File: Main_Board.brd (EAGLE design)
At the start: 122.5 x 95.4 mm, 105 parts, among them J1 SERVO, J5 SPEAKER, J6 SDIO-SDCARD, P1 MOTOR_HEADER, P2 MOTOR_HEADER, P3 JTAG, U1 LMS8117, U10 IMU, U14 TPA2005D1DGN, U2 5V_BUCK_REG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

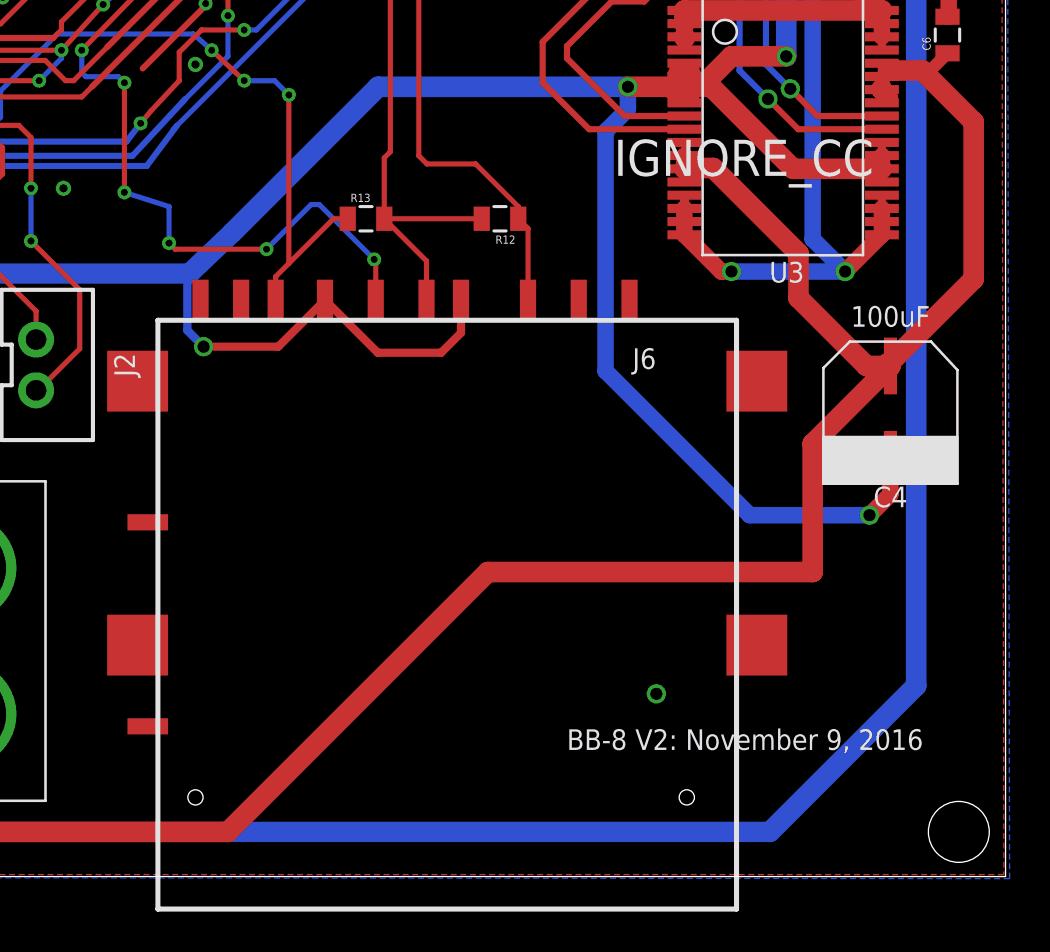
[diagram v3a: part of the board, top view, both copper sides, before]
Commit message: made SD card traces closer in length
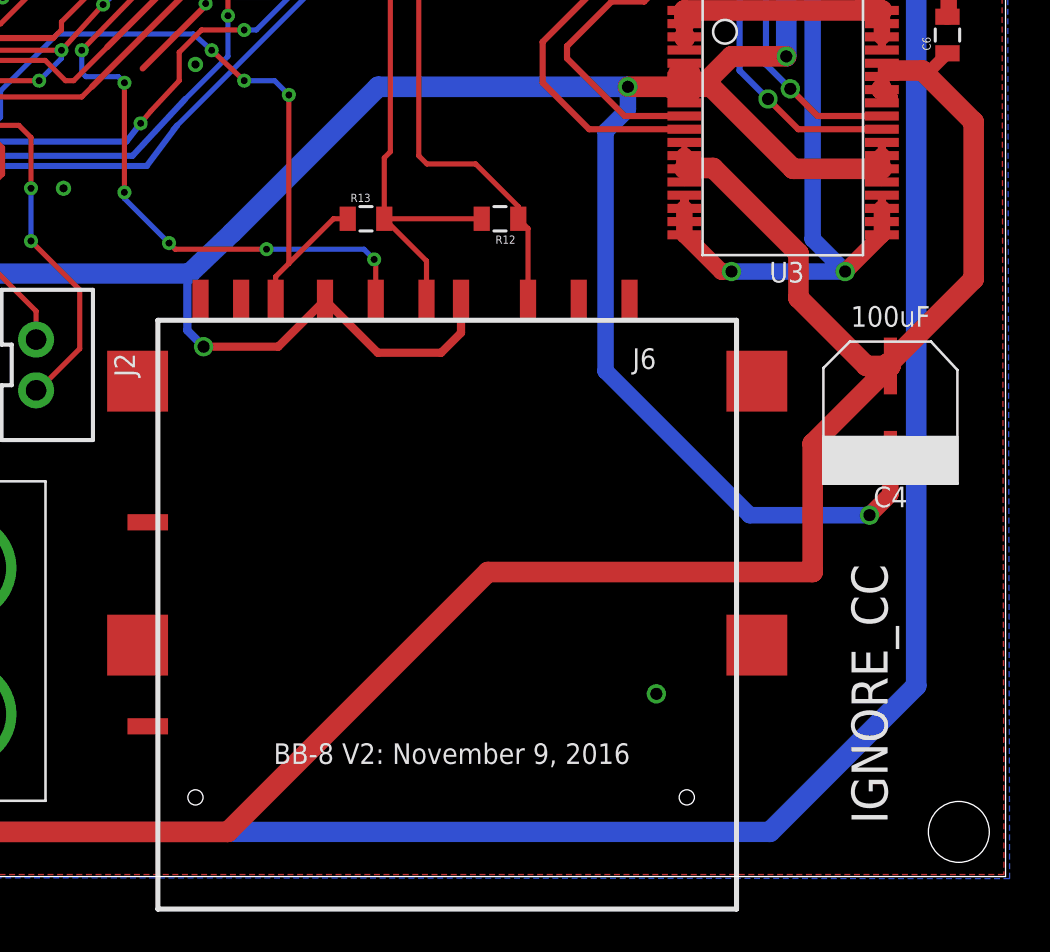
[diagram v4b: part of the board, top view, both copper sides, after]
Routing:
- net SDIO_CK: track 70.6 -> 68.1 mm
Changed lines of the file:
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@@
 <rectangle x1="15.5" y1="83.2" x2="20.7" y2="92.4" layer="41"/>
 <text x="41" y="65.6" size="1.778" layer="21" font="vector">REG_BOOT</text>
-<text x="103.210571875" y="34.512" size="1.778" layer="21" font="vector">IGNORE_CC</text>
+<text x="114.912" y="15.389428125" size="1.778" layer="21" font="vector" rot="R270">IGNORE_CC</text>
 <text x="32.5" y="90.6" size="1.778" layer="21">3.3V</text>
 <text x="32" y="88" size="1.778" layer="21">TX</text>
@@
 Kyle Rakos, Chris Chow
 Alex Marcellus, Allison Gruninger</text>
-<text x="109.671196875" y="6.7455625" size="1.016" layer="21" font="vector" align="center">BB-8 V2: November 9, 2016</text>
+<text x="95.228803125" y="6.0544375" size="1.016" layer="21" font="vector" rot="R180" align="center">BB-8 V2: November 9, 2016</text>
 <rectangle x1="84" y1="17.4" x2="104.8" y2="21.4" layer="41"/>
 <rectangle x1="78.2" y1="22.8" x2="81.3" y2="26" layer="29"/>
@@
 <wire x1="91.48" y1="30.32" x2="91.4" y2="30.4" width="0.254" layer="1"/>
 <via x="91.4" y="30.4" extent="1-16" drill="0.34"/>
-<wire x1="91.4" y1="30.4" x2="88.7" y2="33.1" width="0.254" layer="16"/>
 <wire x1="71.22" y1="50.5" x2="75.4" y2="50.5" width="0.254" layer="1"/>
 <wire x1="79.5" y1="49.9" x2="87.7" y2="58.1" width="0.254" layer="1"/>
@@
 <wire x1="79.1" y1="39.1" x2="79.1" y2="33.7" width="0.254" layer="1"/>
 <via x="79.1" y="33.7" extent="1-16" drill="0.34"/>
-<wire x1="79.1" y1="33.7" x2="81.3" y2="33" width="0.254" layer="16"/>
-<wire x1="81.3" y1="33" x2="81.3" y2="31.2" width="0.254" layer="16"/>
 <via x="81.3" y="31.2" extent="1-16" drill="0.34"/>
 <wire x1="81.3" y1="31.2" x2="81.6" y2="30.9" width="0.254" layer="1"/>
 <wire x1="81.6" y1="30.9" x2="86.1" y2="30.9" width="0.254" layer="1"/>
 <via x="86.1" y="30.9" extent="1-16" drill="0.34"/>
-<wire x1="86.1" y1="30.9" x2="88.3" y2="33.1" width="0.254" layer="16"/>
-<wire x1="88.3" y1="33.1" x2="88.7" y2="33.1" width="0.254" layer="16"/>
 <via x="79.5" y="49.9" extent="1-16" drill="0.34"/>
 <wire x1="79.5" y1="49.9" x2="76" y2="49.9" width="0.254" layer="16"/>
@@
 <wire x1="78.8" y1="39.4" x2="79.1" y2="39.1" width="0.254" layer="16"/>
 <via x="79.1" y="39.1" extent="1-16" drill="0.34"/>
+<wire x1="86.1" y1="30.9" x2="90.9" y2="30.9" width="0.254" layer="16"/>
+<wire x1="90.9" y1="30.9" x2="91.4" y2="30.4" width="0.254" layer="16"/>
+<wire x1="79.1" y1="33.7" x2="79.1" y2="33.4" width="0.254" layer="16"/>
+<wire x1="79.1" y1="33.4" x2="81.3" y2="31.2" width="0.254" layer="16"/>
 </signal>
 <signal name="SDIO_CMD">

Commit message: Gerbers, new DRU, and finished board (hopefully)
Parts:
- removed LED4: (no value), LilyPad-Wearables:LED-1206
- added POWER: (no value), LilyPad-Wearables:LED-1206
- J2: value (none) -> 2-PIN-JUMPER
- moved R74 127.8 mm to (112.8, 80.0), turned to 270 degrees
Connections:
- net GND: now also POWER.C; no longer LED4.C, U8.P$16, U8.P$9
- net N$42: now also POWER.A; no longer LED4.A
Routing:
- net 3.3V: track 435.1 -> 425.1 mm, vias 22 -> 20
- net GND: track 593.6 -> 596.3 mm
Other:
- board text added: "BB-8 V2: November 10, 2016"
- board text removed: "BB-8 V2: November 9, 2016"

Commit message: Added decoupling caps near level translators
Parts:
- added C12, C13: .1uF, SparkFun-Capacitors:0805
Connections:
- net 3.3V: now also C13.1
- net 5V: now also C12.1
- net GND: now also C12.2, C13.2
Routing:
- net 5V: track 279.4 -> 282.9 mm
- net 3.3V: track 425.1 -> 426.5 mm
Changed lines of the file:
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@@
 <element name="R15" library="SparkFun-Resistors" package="0805" value="100" x="68.2" y="69.6" rot="R180"/>
 <element name="J3" library="SparkFun-Connectors" package="1X01_NO_SILK" value="" x="66.8" y="66.1"/>
+<element name="C12" library="SparkFun-Capacitors" package="0805" value=".1uF" x="96.1" y="67.8"/>
+<element name="C13" library="SparkFun-Capacitors" package="0805" value=".1uF" x="57.5" y="36" rot="R270"/>
 </elements>
 <signals>
@@
 <wire x1="92.25" y1="70.35" x2="92.3" y2="70.3" width="0.3048" layer="1"/>
 <wire x1="92.3" y1="70.3" x2="93.6" y2="70.3" width="0.3048" layer="1"/>
-<wire x1="93.6" y1="70.3" x2="94.2" y2="69.7" width="0.3048" layer="1"/>
+<wire x1="93.6" y1="70.3" x2="93.9" y2="70" width="0.3048" layer="1"/>
+<wire x1="93.9" y1="70" x2="94.2" y2="69.7" width="0.3048" layer="1"/>
 <wire x1="5.4" y1="55.87" x2="2.4" y2="52.87" width="0.8128" layer="1"/>
 <wire x1="17.5" y1="6.58" x2="17.5" y2="10.8" width="1" layer="1"/>
@@
 <wire x1="16.2" y1="32.9" x2="16.1" y2="33" width="1.016" layer="1"/>
 <wire x1="16.1" y1="33" x2="16.1" y2="37.3" width="1.016" layer="1"/>
+<contactref element="C12" pad="1"/>
+<wire x1="95.2" y1="67.8" x2="93.9" y2="67.8" width="0.4064" layer="1"/>
+<wire x1="93.9" y1="67.8" x2="93.9" y2="70" width="0.4064" layer="1"/>
 </signal>
 <signal name="N$8">
@@
 <wire x1="98.7" y1="77.9" x2="99.9" y2="79.1" width="0.4064" layer="1"/>
 <wire x1="99.9" y1="79.1" x2="112.8" y2="79.1" width="0.4064" layer="1"/>
+<contactref element="C13" pad="1"/>
+<wire x1="57.5" y1="36.9" x2="57.6" y2="36.9" width="0.4064" layer="1"/>
+<wire x1="57.6" y1="36.9" x2="57.6" y2="38.25" width="0.4064" layer="1"/>
 </signal>
 <signal name="N$15">
@@
 <wire x1="109" y1="86" x2="109.5" y2="86.5" width="0.4064" layer="1"/>
 <wire x1="109.5" y1="86.5" x2="112.8" y2="86.5" width="0.4064" layer="1"/>
+<contactref element="C13" pad="2"/>
+<contactref element="C12" pad="2"/>
 </signal>
 <signal name="N$136">

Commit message: updated the library
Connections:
- net GND: now also U8.P$16, U8.P$9
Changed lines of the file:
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@@
 <contactref element="C13" pad="2"/>
 <contactref element="C12" pad="2"/>
+<contactref element="U8" pad="P$9"/>
+<contactref element="U8" pad="P$16"/>
 </signal>
 <signal name="N$136">
